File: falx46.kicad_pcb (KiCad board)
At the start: 2 copper layers, 281.1 x 112.1 mm, 140 parts, among them J1 USB_C_Receptacle_USB2.0, J2 OLED_I2C, J3 AVR-ISP-6, J4 GLOVE_I2C, J5 TRRS_I2C, SW1 SW_PUSH, SW10 SW_PUSH, SW11 SW_PUSH, SW12 SW_PUSH, SW13 SW_PUSH, SW14 SW_PUSH, SW15 SW_PUSH, SW16 SW_PUSH, SW17 SW_PUSH, SW18 SW_PUSH, SW19 Rotary_Encoder_Switch, SW2 SW_PUSH, SW20 SW_PUSH, SW21 SW_PUSH, SW22 SW_PUSH, SW23 SW_PUSH, SW24 SW_PUSH, SW25 SW_PUSH, SW26 SW_PUSH, SW27 SW_PUSH, SW28 SW_PUSH, SW29 SW_PUSH, SW3 SW_PUSH, SW30 SW_PUSH, SW31 SW_PUSH, SW32 SW_PUSH, SW33 SW_PUSH, SW34 SW_PUSH, SW35 SW_PUSH, SW36 Rotary_Encoder_Switch, SW37 SW_PUSH, SW38 SW_PUSH, SW39 SW_PUSH, SW4 SW_PUSH, SW40 SW_PUSH, SW41 SW_PUSH, SW42 SW_PUSH, SW43 SW_PUSH, SW44 SW_PUSH, SW45 SW_PUSH, SW46 SW_PUSH, SW47 SW_Push, SW5 SW_PUSH, SW6 SW_PUSH, SW7 SW_PUSH, SW8 SW_PUSH, SW9 SW_PUSH, U1 ATmega32U4-AU, Y1 16MHz

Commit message: 一旦配線を完了
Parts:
- SW1, SW10, SW11, SW12, SW13, SW14, SW15, SW16, SW17, SW18, SW2, SW20, SW21, SW22, SW23, SW24, SW25, SW26, SW27, SW28, SW29, SW3, SW30, SW31, SW32, SW33, SW34, SW35, SW37, SW38, SW39, SW4, SW40, SW41, SW42, SW43, SW44, SW45, SW46, SW5, SW6, SW7, SW8, SW9: footprint 1m38_kbd:MXOnly-1U-Hotswap-Antishear-mod -> 1m38_kbd:CherryMX_Hotswap_mod
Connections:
- D43 pad 1: COL6 -> ROWR3
- D44 pad 1: COL6 -> ROWR3
- D45 pad 1: COL6 -> ROWR3
- D46 pad 1: COL6 -> ROWR3
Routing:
- net COL6: track 177.9 -> 91.2 mm, vias 4 -> 0
- net ROWR3: track 0.00 -> 64.9 mm, vias 0 -> 2
- net COL4: track 117.0 -> 127.7 mm
- net UCAP: track 0.00 -> 9.99 mm, vias 0 -> 2
- net Net-(LED4-Pad3): track 80.1 -> 70.2 mm
- net COL5: track 114.2 -> 123.9 mm
- net Net-(LED2-Pad3): track 91.1 -> 99.6 mm, vias 6 -> 5
- net COL1: track 70.1 -> 77.7 mm
- net COL3: track 211.4 -> 218.5 mm
- net Net-(LED10-Pad3): track 67.1 -> 60.6 mm
- net COL2: track 73.7 -> 79.9 mm
- net GND: track 915.0 -> 918.7 mm
- net COL0: track 35.8 -> 38.1 mm
- net HWB: track 15.0 -> 12.8 mm, vias 2 -> 0
- net Net-(LED10-Pad4): track 64.1 -> 65.7 mm
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
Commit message: 配線完了
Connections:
- D24 pad 1: ROWR0 -> MISO
- D25 pad 1: ROWR0 -> MISO
- D26 pad 1: ROWR0 -> MISO
- D27 pad 1: ROWR0 -> MISO
- D28 pad 1: ROWR0 -> MISO
- D29 pad 1: ROWR1 -> MOSI
- D30 pad 1: ROWR1 -> MOSI
- D31 pad 1: ROWR1 -> MOSI
- D32 pad 1: ROWR1 -> MOSI
- D33 pad 1: ROWR1 -> MOSI
- D34 pad 1: ROWR1 -> MOSI
- D35 pad 1: ROWR1 -> MOSI
- J3 pad 3: SCK -> ROWR2
- U1 pad 21: Net-(U1-Pad21) -> COL0
- U1 pad 22: Net-(U1-Pad22) -> COL1
- U1 pad 25: Net-(U1-Pad25) -> COL2
- U1 pad 26: Net-(U1-Pad26) -> COL3
- U1 pad 27: Net-(U1-Pad27) -> COL4
- U1 pad 28: Net-(U1-Pad28) -> COL5
- U1 pad 29: Net-(U1-Pad29) -> COL6
- U1 pad 30: Net-(U1-Pad30) -> LED
- U1 pad 31: Net-(U1-Pad31) -> ROWL3
- U1 pad 32: Net-(U1-Pad32) -> ROWL2
- U1 pad 36: Net-(U1-Pad36) -> ROWL1
- U1 pad 37: Net-(U1-Pad37) -> ROWL0
- U1 pad 38: Net-(U1-Pad38) -> ENCL1
- U1 pad 39: Net-(U1-Pad39) -> ENCL2
- U1 pad 40: Net-(U1-Pad40) -> ENCR2
- U1 pad 41: Net-(U1-Pad41) -> ENCR1
- U1 pad 8: Net-(U1-Pad8) -> ROWR3
- U1 pad 9: SCK -> ROWR2
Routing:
- net COL0: track 38.1 -> 367.0 mm, vias 0 -> 8
- net COL1: track 77.7 -> 363.9 mm, vias 2 -> 8
- net COL2: track 79.9 -> 341.4 mm, vias 0 -> 7
- net ROWR2: track 141.0 -> 317.2 mm, vias 2 -> 7
- net MOSI: track 142.2 -> 311.1 mm, vias 3 -> 7
- net COL4: track 127.7 -> 290.9 mm, vias 0 -> 5
- net SCK: track 147.4 -> 0.00 mm, vias 3 -> 0
- net MISO: track 160.0 -> 303.1 mm, vias 5 -> 11
- net ROWR1: track 142.2 -> 0.00 mm, vias 2 -> 0
- net COL3: track 218.5 -> 335.4 mm, vias 2 -> 5
- net COL5: track 123.9 -> 240.2 mm, vias 0 -> 3
- net ROWR0: track 109.5 -> 0.00 mm, vias 4 -> 0
- net ROWL0: track 100.7 -> 179.2 mm, vias 6 -> 8
- net COL6: track 91.2 -> 159.7 mm, vias 0 -> 5
- net ROWL1: track 139.8 -> 198.8 mm, vias 0 -> 2
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- added copper zone on B.Cu, net GND
- added copper zone on F.Cu, net GND

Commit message: シルク調整中
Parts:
- D1, D10, D11, D12, D13, D14, D15, D16, D17, D18, D19, D2, D20, D21, D22, D23, D24, D25, D26, D27, D28, D29, D3, D30, D31, D32, D33, D34, D35, D36, D37, D38, D39, D4, D40, D41, D42, D43, D44, D45, D46, D5, D6, D7, D8, D9: footprint foostan-kbd:D3_SMD_v2 -> 1m38_kbd:D3_SMD_v2_silk
- J1, SW47: moved to F.Cu
- J5: footprint 1m38_kbd:MJ-4PP-9_1side_backside-mask -> 1m38_kbd:MJ-4PP-9_1side_no-mask
- moved J1 5.98 mm to (30.3, 46.7), turned to 270 degrees
- moved R1 2.83 mm to (38.2, 48.4)
- moved R2 2.80 mm to (38.2, 50.9)
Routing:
- net GND: track 921.6 -> 934.5 mm, vias 10 -> 13
- net Net-(J1-PadB5): track 24.2 -> 18.3 mm, vias 3 -> 1
- net /DUP: track 239.4 -> 237.7 mm
- net Net-(J1-PadA5): track 8.16 -> 7.01 mm
- net Net-(F1-Pad2): track 28.1 -> 28.9 mm
- net /DUN: track 235.9 -> 235.6 mm, vias 4 -> 3

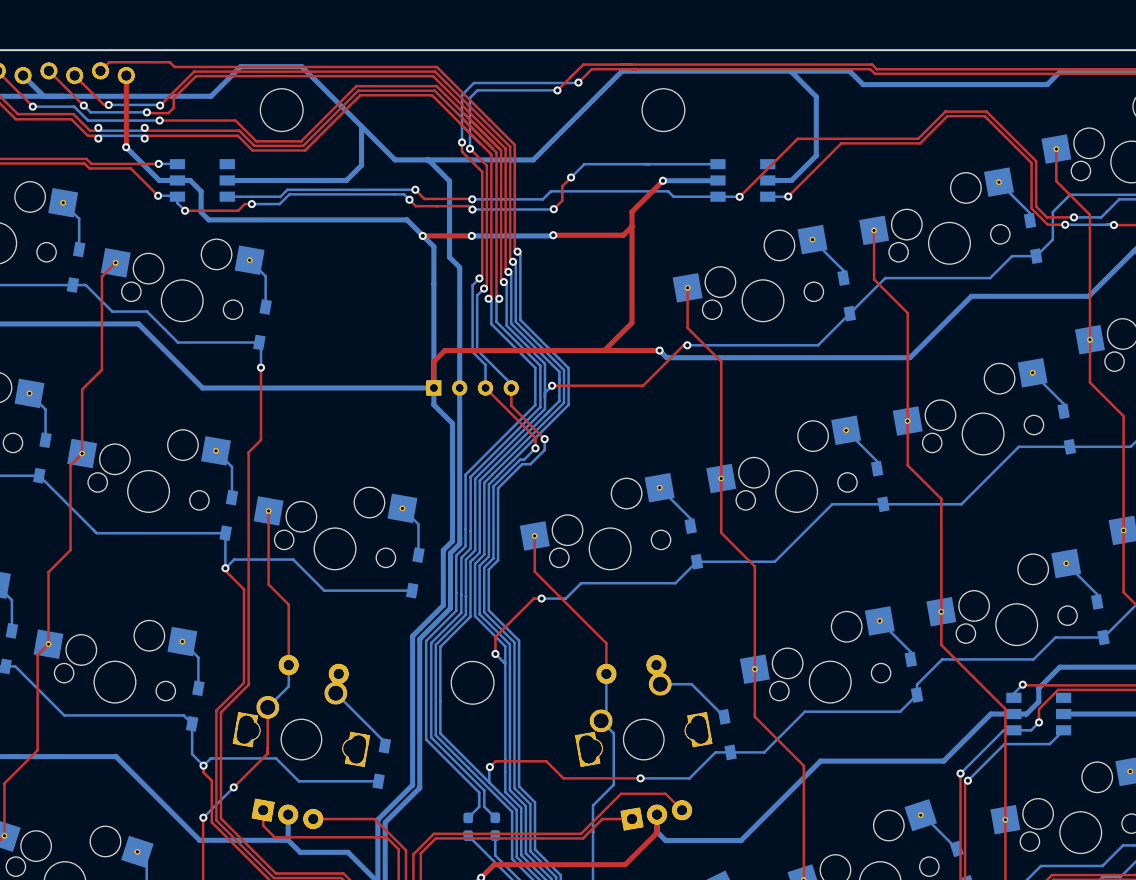
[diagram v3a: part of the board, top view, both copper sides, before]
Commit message: oled用ネジ穴追加、各種調整、クレジット追加
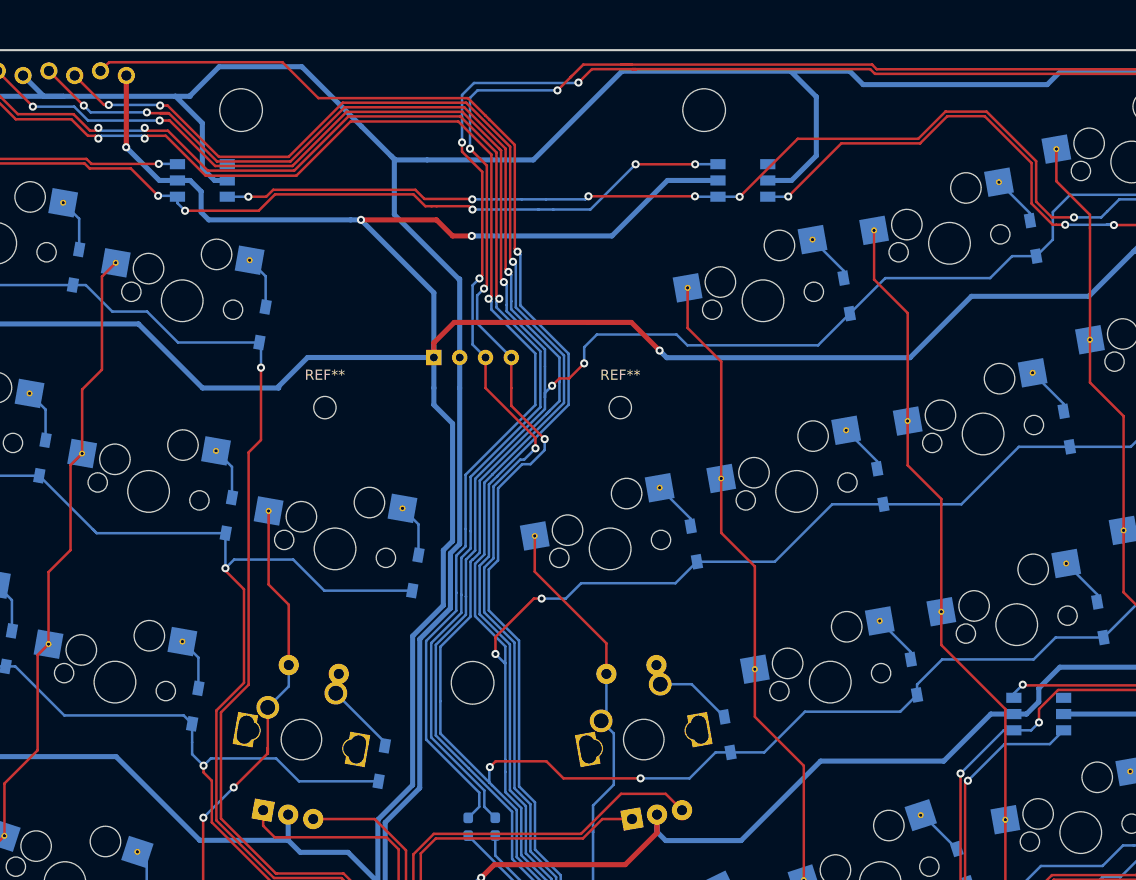
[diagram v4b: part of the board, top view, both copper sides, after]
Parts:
- added REF**: MountingHole_2.2mm_M2, MountingHole:MountingHole_2.2mm_M2, F.Cu at (179.3, 61.1)
- added REF**: MountingHole_2.2mm_M2, MountingHole:MountingHole_2.2mm_M2, F.Cu at (150.2, 61.1)
- moved HOLE6 4.00 mm to (142.0, 31.8)
- moved HOLE7 4.00 mm to (187.6, 31.8)
- moved J2 3.00 mm to (164.8, 57.5)
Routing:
- net GND: track 934.5 -> 926.1 mm, vias 13 -> 11
- net VBUS: track 862.2 -> 857.6 mm
- net /DUP: track 237.7 -> 233.6 mm
- net /DUN: track 235.6 -> 232.8 mm
- net MISO: track 303.1 -> 300.4 mm
- net MOSI: track 311.1 -> 312.6 mm
- net ROWR2: track 317.2 -> 318.4 mm
- net Net-(LED6-Pad3): track 104.6 -> 103.4 mm, vias 8 -> 6
- net Net-(LED7-Pad3): track 108.2 -> 107.6 mm, vias 4 -> 6
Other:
- board text added: "yacc46 v0.1 designed by 1.038"
